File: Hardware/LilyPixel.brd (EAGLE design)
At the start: 20 x 20 mm, 13 parts

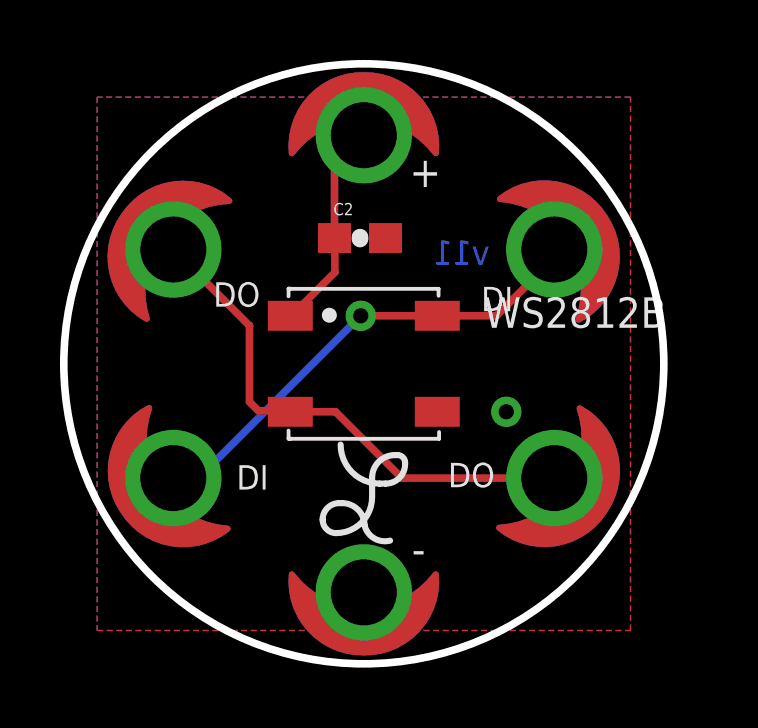
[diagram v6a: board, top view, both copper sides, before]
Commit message: Fixed qc checklist problems
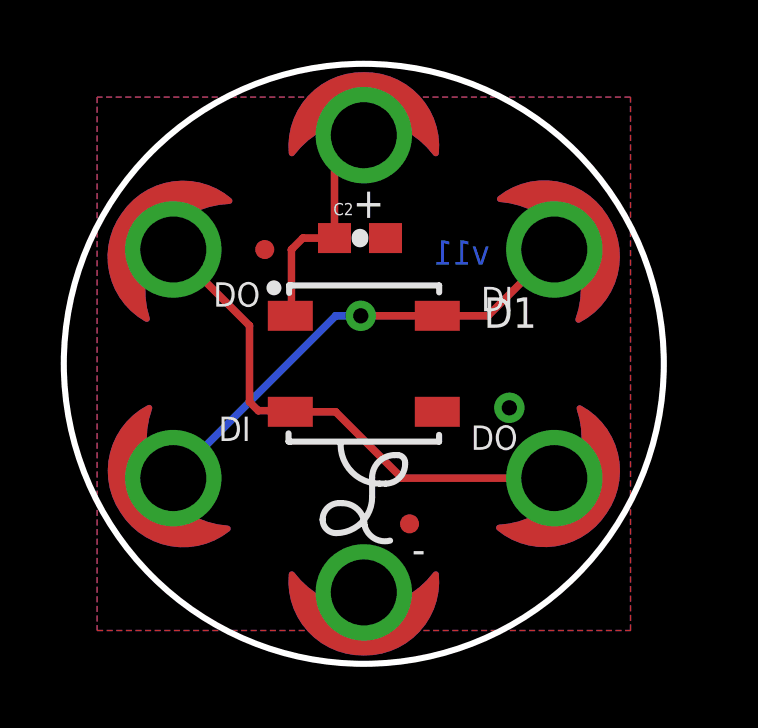
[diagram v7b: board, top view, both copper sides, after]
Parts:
- removed U$2: (no value), SparkFun-Aesthetics:SFE_LOGO_FLAME_.1
- added FID1, FID2: FIDUCIALUFIDUCIAL, SparkFun-Aesthetics:MICRO-FIDUCIAL
- added LOGO2: SFE_LOGO_FLAME.1_INCH, SparkFun-Aesthetics:SFE_LOGO_FLAME_.1
- D1: value (none) -> WS2812B
- renumbered WS2812B to D1
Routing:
- net VCC: track 7.07 -> 7.69 mm
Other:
- board text added: "Board Note: Purple 0.8mm PCB"
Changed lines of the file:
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@@
 <setting verticaltext="up"/>
 </settings>
-<grid distance="0.05" unitdist="inch" unit="inch" style="lines" multiple="1" display="yes" altdistance="0.001" altunitdist="inch" altunit="inch"/>
+<grid distance="0.05" unitdist="inch" unit="inch" style="lines" multiple="1" display="yes" altdistance="0.0001" altunitdist="inch" altunit="inch"/>
 <layers>
 <layer number="1" name="Top" color="4" fill="1" visible="yes" active="yes"/>
@@
 <layer number="27" name="tValues" color="7" fill="1" visible="no" active="yes"/>
 <layer number="28" name="bValues" color="7" fill="1" visible="no" active="yes"/>
-<layer number="29" name="tStop" color="7" fill="3" visible="no" active="yes"/>
+<layer number="29" name="tStop" color="7" fill="3" visible="yes" active="yes"/>
 <layer number="30" name="bStop" color="7" fill="6" visible="no" active="yes"/>
 <layer number="31" name="tCream" color="7" fill="4" visible="no" active="yes"/>
@@
 <layer number="37" name="tTest" color="7" fill="1" visible="no" active="no"/>
 <layer number="38" name="bTest" color="7" fill="1" visible="no" active="no"/>
-<layer number="47" name="Measures" color="7" fill="1" visible="no" active="no"/>
+<layer number="47" name="Measures" color="7" fill="1" visible="yes" active="yes"/>
 <layer number="48" name="Document" color="7" fill="1" visible="no" active="no"/>
 <layer number="49" name="Reference" color="7" fill="1" visible="no" active="no"/>
@@
 <layer number="111" name="LPC17xx" color="7" fill="1" visible="no" active="yes"/>
 <layer number="112" name="tSilk" color="7" fill="1" visible="no" active="yes"/>
+<layer number="113" name="IDFDebug" color="4" fill="1" visible="yes" active="yes"/>
 <layer number="116" name="Patch_BOT" color="9" fill="4" visible="no" active="no"/>
 <layer number="121" name="_tsilk" color="7" fill="1" visible="no" active="no"/>
@@
 <wire x1="-2.91" y1="-5.04" x2="-5.82" y2="0" width="0.2032" layer="42" curve="-184.522199"/>
 <wire x1="-5.82" y1="0" x2="-2.93" y2="5.05" width="0.2032" layer="42" curve="-184.554034"/>
-<circle x="-1.27" y="2.54" radius="0.508" width="0.254" layer="30"/>
-<circle x="1.27" y="2.54" radius="0.5236" width="0.254" layer="30"/>
-<circle x="1.27" y="0" radius="0.5236" width="0.254" layer="30"/>
-<circle x="-1.27" y="0" radius="0.508" width="0.254" layer="30"/>
-<circle x="-1.27" y="-2.54" radius="0.5236" width="0.254" layer="30"/>
-<circle x="1.27" y="-2.54" radius="0.508" width="0.254" layer="30"/>
 <circle x="0" y="0" radius="7.5" width="0.0508" layer="47"/>
 <circle x="0" y="0" radius="5.8309" width="0.0508" layer="47"/>
 <circle x="0" y="0" radius="4.5" width="0.0508" layer="47"/>
-<circle x="0" y="0" radius="10" width="0.254" layer="20"/>
-<text x="1.524" y="5.8928" size="1.016" layer="21" font="vector" ratio="15">+</text>
+<circle x="0" y="0" radius="10" width="0.2032" layer="20"/>
+<text x="-0.3657625" y="4.8641" size="1.016" layer="21" font="vector" ratio="15">+</text>
 <text x="1.6002" y="-6.6802" size="1.016" layer="21" font="vector" ratio="15">-</text>
 <text x="33.02" y="-33.02" size="1.778" layer="27" font="vector" ratio="15">M. HORD</text>
@@
 </polygon>
 <text x="-3.4544" y="2.7178" size="0.8128" layer="21" font="vector" ratio="15" rot="R180">DO</text>
-<text x="4.3688" y="-3.302" size="0.8128" layer="21" font="vector" ratio="15" rot="R180">DO</text>
+<text x="5.1308" y="-2.0548625" size="0.8128" layer="21" font="vector" ratio="15" rot="R180">DO</text>
 <text x="3.9116" y="1.7526" size="0.8128" layer="21" font="vector" ratio="15">DI</text>
-<text x="-3.175" y="-3.3782" size="0.8128" layer="21" font="vector" ratio="15" rot="R180">DI</text>
+<text x="-3.7719" y="-1.760221875" size="0.8128" layer="21" font="vector" ratio="15" rot="R180">DI</text>
 <text x="4.191" y="3.302" size="0.8128" layer="16" font="vector" ratio="15" rot="MR0">v11</text>
 <text x="3.81" y="-25.4" size="1.778" layer="51" font="vector" ratio="10">Mike Hord</text>
 <text x="-15.24" y="-27.94" size="1.778" layer="51" font="vector" ratio="10">Revised by: Patrick Alberts</text>
+<text x="-20.32" y="-13.97" size="1.778" layer="51" font="vector" ratio="10">Board Note: Purple 0.8mm PCB</text>
+<dimension x1="-15.24" y1="-10.16" x2="-15.24" y2="10.16" x3="-16.51" y3="0" textsize="1.778" textratio="10" layer="47"/>
+<dimension x1="-10.16" y1="12.7" x2="8.89" y2="12.7" x3="-0.635" y3="13.97" textsize="1.778" textratio="10" layer="47"/>
 </plain>
 <attributes>
@@
 <element name="FRAME1" library="SparkFun-Aesthetics" package="CREATIVE_COMMONS" value="FRAME-LETTER" x="-26.67" y="-25.4"/>
 <element name="U$1" library="LilyPad-Wearables" package="LOGO-LILYPAD" value="LOGO-LPLP" x="0" y="0" rot="MR0"/>
-<element name="WS2812B" library="SparkFun-LED" package="WS2812B" value="" x="0" y="0"/>
+<element name="D1" library="SparkFun-LED" package="WS2812B" value="WS2812B" x="0" y="0"/>
 <element name="JP4" library="LilyPad-Wearables" package="PETAL-SMALL-2SIDE" value="SEWTAP6" x="0" y="7.62" rot="R180"/>
 <element name="JP5" library="LilyPad-Wearables" package="PETAL-SMALL-2SIDE" value="SEWTAP6" x="6.35" y="3.81" rot="SR123"/>
@@
 <element name="JP6" library="LilyPad-Wearables" package="PETAL-SMALL-2SIDE" value="SEWTAP6" x="-6.35" y="-3.81" rot="R303"/>
 <element name="LOGO1" library="SparkFun-Aesthetics" package="OSHW-LOGO-S" value="OSHW-LOGOS" x="0" y="3.81" rot="MR0"/>
-<element name="U$2" library="SparkFun-Aesthetics" package="SFE_LOGO_FLAME_.1" value="" x="1.016" y="-6.096" rot="MR0"/>
+<element name="LOGO2" library="SparkFun-Aesthetics" package="SFE_LOGO_FLAME_.1" value="SFE_LOGO_FLAME.1_INCH" x="1.143" y="-6.223" rot="MR0"/>
+<element name="FID1" library="SparkFun-Aesthetics" package="MICRO-FIDUCIAL" value="FIDUCIALUFIDUCIAL" x="1.524" y="-5.334"/>
+<element name="FID2" library="SparkFun-Aesthetics" package="MICRO-FIDUCIAL" value="FIDUCIALUFIDUCIAL" x="-3.302" y="3.81"/>
 </elements>
 <signals>
 <signal name="VCC">
 <contactref element="C2" pad="1"/>
-<contactref element="WS2812B" pad="1"/>
+<contactref element="D1" pad="1"/>
 <contactref element="JP4" pad="1"/>
 <wire x1="-0.977" y1="4.191" x2="-0.977" y2="6.643" width="0.254" layer="1"/>
 <wire x1="-0.977" y1="6.643" x2="0" y2="7.62" width="0.254" layer="1"/>
 <wire x1="-2.45" y1="1.6" x2="-2.4132" y2="1.6" width="0.254" layer="1"/>
-<wire x1="-2.4132" y1="1.6" x2="-0.9652" y2="3.048" width="0.254" layer="1"/>
-<wire x1="-0.9652" y1="3.048" x2="-0.9652" y2="4.1792" width="0.254" layer="1"/>
 <wire x1="-0.9652" y1="4.1792" x2="-0.977" y2="4.191" width="0.254" layer="1"/>
+<wire x1="-2.4132" y1="1.6" x2="-2.4132" y2="3.8098" width="0.254" layer="1"/>
+<wire x1="-2.4132" y1="3.8098" x2="-2.032" y2="4.191" width="0.254" layer="1"/>
+<wire x1="-2.032" y1="4.191" x2="-0.977" y2="4.191" width="0.254" layer="1"/>
 </signal>
 <signal name="GND">
@@
 </polygon>
 <contactref element="C2" pad="2"/>
-<contactref element="WS2812B" pad="3"/>
+<contactref element="D1" pad="3"/>
 <contactref element="JP3" pad="1"/>
-<via x="4.7498" y="-1.6002" extent="1-16" drill="0.508"/>
+<via x="4.8514" y="-1.465578125" extent="1-16" drill="0.508"/>
 </signal>
 <signal name="N$7">
@@
 <signal name="DI1">
 <contactref element="JP5" pad="1"/>
-<contactref element="WS2812B" pad="4"/>
+<contactref element="D1" pad="4"/>
 <contactref element="JP6" pad="1"/>
-<wire x1="6.35" y1="3.81" x2="6.35" y2="3.5306" width="0.254" layer="1"/>
-<wire x1="6.35" y1="3.5306" x2="4.4196" y2="1.6002" width="0.254" layer="1"/>
-<wire x1="4.4196" y1="1.6002" x2="2.4502" y2="1.6002" width="0.254" layer="1"/>
 <wire x1="2.4502" y1="1.6002" x2="2.45" y2="1.6" width="0.254" layer="1"/>
 <via x="-0.1016" y="1.6002" extent="1-16" drill="0.508"/>
 <wire x1="-0.1016" y1="1.6002" x2="2.4498" y2="1.6002" width="0.254" layer="1"/>
 <wire x1="2.4498" y1="1.6002" x2="2.45" y2="1.6" width="0.254" layer="1"/>
-<wire x1="-6.35" y1="-3.81" x2="-5.5118" y2="-3.81" width="0.254" layer="16"/>
-<wire x1="-5.5118" y1="-3.81" x2="-0.1016" y2="1.6002" width="0.254" layer="16"/>
+<wire x1="6.35" y1="3.81" x2="4.14" y2="1.6" width="0.254" layer="1"/>
+<wire x1="4.14" y1="1.6" x2="2.45" y2="1.6" width="0.254" layer="1"/>
+<wire x1="-6.35" y1="-3.81" x2="-0.9398" y2="1.6002" width="0.254" layer="16"/>
+<wire x1="-0.9398" y1="1.6002" x2="-0.1016" y2="1.6002" width="0.254" layer="16"/>
 </signal>
 <signal name="DO1">
 <contactref element="JP2" pad="1"/>
-<contactref element="WS2812B" pad="2"/>
+<contactref element="D1" pad="2"/>
 <contactref element="JP1" pad="1"/>
 <wire x1="-2.45" y1="-1.6" x2="-0.94" y2="-1.6" width="0.254" layer="1"/>
